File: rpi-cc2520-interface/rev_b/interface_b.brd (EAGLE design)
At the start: 30.5 x 39.5 mm, 5 parts, among them J1 PINHD-2X12/SMD, J2 PINHD-2X12/SMD

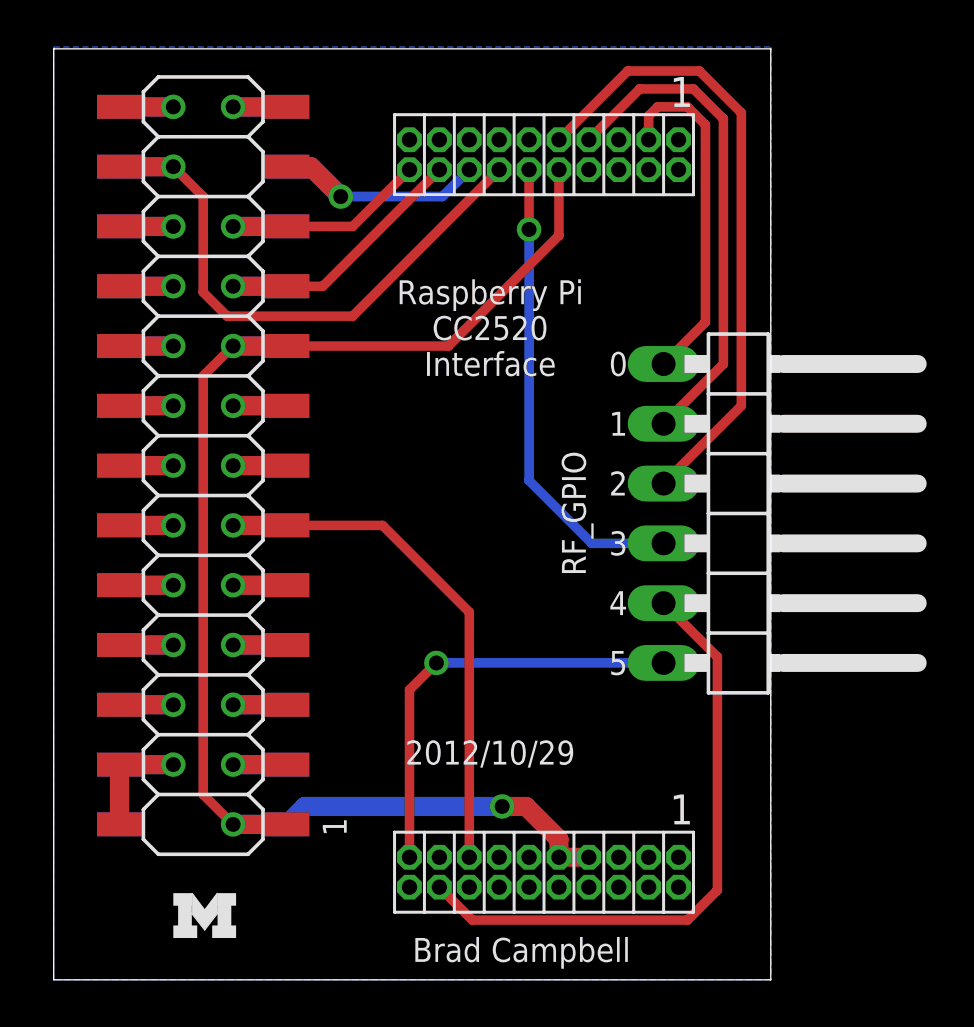
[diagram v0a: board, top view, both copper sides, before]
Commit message: new rpi-cc2520 board is routed. want to add pin labels
git-svn-id: svn+ssh://energy.eecs.umich.edu/svnroot/shed/projects/pi-router/eagle@2756 d5a83394-2863-40c7-9603-03341d4c7fdc
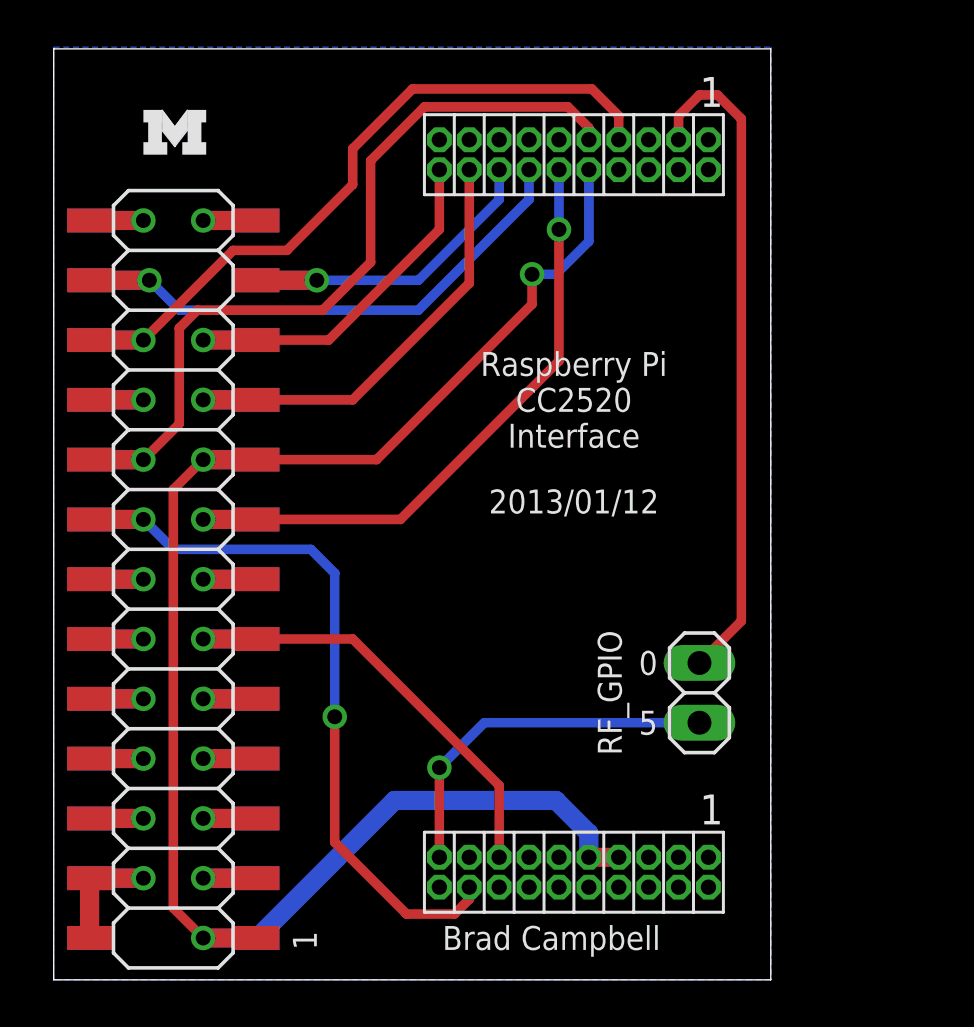
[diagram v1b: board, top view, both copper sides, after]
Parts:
- JP1: device pinhead:1X06/90 -> pinhead:1X02
- moved U$1 33.3 mm to (3.81, 35.1)
- moved JP1 7.96 mm to (27.4, 12.2), turned to 90 degrees
- moved J1 4.99 mm to (5.08, 17.0)
- moved J2 4.99 mm to (5.08, 17.0)
- moved EVM1 1.27 mm to (22.1, 19.8)
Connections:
- removed net GPIO22: J1.16, J2.15
- removed net GPIO23: J1.15, J2.16
- removed net GPIO24: J1.17, J2.18
- removed net GPIO25: J1.21, J2.22
- removed net RF_GPIO0: EVM1.P1_3, JP1.1
- removed net RF_GPIO1: EVM1.P1_7, JP1.2
- removed net RF_GPIO2: EVM1.P1_9, JP1.3
- removed net RF_GPIO3: EVM1.P1_12, JP1.4
- removed net RF_GPIO4: EVM1.P2_18, JP1.5
- removed net RF_GPIO5: EVM1.P2_19, JP1.6
- new net CCA: EVM1.P1_12, J1.16, J2.15
- new net CC_GPIO0: EVM1.P1_3, JP1.2
- new net CC_GPIO5: EVM1.P2_19, JP1.1
- new net FIFO: EVM1.P1_7, J1.21, J2.22
- new net FIFOP: EVM1.P1_9, J1.17, J2.18
- new net SFD: EVM1.P2_18, J1.15, J2.16
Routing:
- net FIFOP: track 0.00 -> 35.5 mm, vias 0 -> 1
- net SFD: track 0.00 -> 32.8 mm, vias 0 -> 2
- net FIFO: track 0.00 -> 31.6 mm, vias 0 -> 1
- net CC_GPIO0: track 0.00 -> 28.3 mm
- net CCA: track 0.00 -> 28.3 mm, vias 0 -> 2
- net RF_GPIO2: track 26.8 -> 0.00 mm
- net RF_GPIO4: track 26.1 -> 0.00 mm
- net RF_GPIO1: track 21.1 -> 0.00 mm
- net RF_GPIO3: track 20.0 -> 0.00 mm, vias 1 -> 0
- net RF_GPIO5: track 18.4 -> 0.00 mm, vias 1 -> 0
- net CC_GPIO5: track 0.00 -> 15.6 mm, vias 0 -> 1
- net RF_GPIO0: track 14.8 -> 0.00 mm
- net 3.3V: track 61.3 -> 71.6 mm
- net MOSI: track 13.1 -> 20.5 mm
- net MISO: track 10.8 -> 16.8 mm
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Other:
- board text added: "2013/01/12"
- board text removed: "2"
- board text removed: "2012/10/29"
- board text removed: "3"
- board text removed: "4"

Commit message: added LEDS and pin labels to interface board
git-svn-id: svn+ssh://energy.eecs.umich.edu/svnroot/shed/projects/pi-router/eagle@2765 d5a83394-2863-40c7-9603-03341d4c7fdc
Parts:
- added D1, D2, D3: (no value), SparkFun-LED:LED-0603
- added R1, R2, R3: (no value), rcl:R0603
- moved U$1 1.02 mm to (3.81, 36.1)
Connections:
- removed net 3.3V: EVM1.P1_10, EVM1.P2_7, EVM1.P2_9, J1.18, J1.2, J2.1, J2.17
- removed net GPIO18: J1.11, J2.12
- removed net GPIO27: J1.14, J2.13
- removed net GPIO4: J1.8, J2.7
- new net LED0: J1.8, J2.7, R1.1
- new net LED1: J1.11, J2.12, R2.1
- new net LED2: J1.14, J2.13, R3.1
- new net N$1: D1.C, R1.2
- new net N$2: D2.C, R2.2
- new net N$3: D3.C, R3.2
- new net VCC: D1.A, D2.A, D3.A, EVM1.P1_10, EVM1.P2_7, EVM1.P2_9, J1.18, J1.2, J2.1, J2.17
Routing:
- net VCC: track 0.00 -> 99.5 mm, vias 0 -> 3
- net 3.3V: track 71.6 -> 0.00 mm, vias 3 -> 0
- net LED2: track 0.00 -> 33.5 mm, vias 0 -> 3
- net LED1: track 0.00 -> 31.2 mm, vias 0 -> 3
- net LED0: track 0.00 -> 18.3 mm, vias 0 -> 2
- net GPIO18: track 4.57 -> 0.00 mm, vias 1 -> 0
- net GPIO4: track 4.57 -> 0.00 mm, vias 1 -> 0
- net GPIO27: track 4.57 -> 0.00 mm, vias 1 -> 0
- net N$2: track 0.00 -> 2.74 mm, vias 0 -> 1
- net N$1: track 0.00 -> 2.73 mm, vias 0 -> 1
- net N$3: track 0.00 -> 2.46 mm, vias 0 -> 1
- net SFD: track 32.8 -> 32.1 mm
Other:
- board text added: "2013/01/14"
- board text added: "3.3V"
- board text added: "5V"
- board text added: "CCA"
- board text added: "CE1"
- board text added: "CS"
- board text added: "FIFO"
- board text added: "FIFP"
- board text added: "G17"
- board text added: "GND"
- board text added: "LE1"
- board text added: "LED0"
- board text added: "LED2"
- board text added: "MISO"
- board text added: "MOSI"
- board text added: "RXD"
- board text added: "SCL"
- board text added: "SCLK"
- board text added: "SDA"
- board text added: "SFD"
- board text added: "TXD"
- board text removed: "2013/01/12"

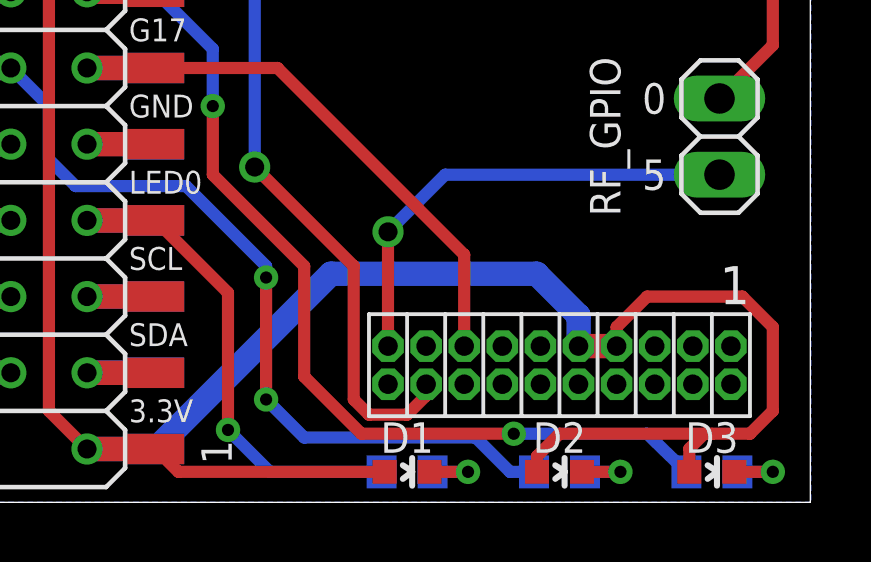
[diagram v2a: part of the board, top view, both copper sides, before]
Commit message: fixed an airwire
git-svn-id: svn+ssh://energy.eecs.umich.edu/svnroot/shed/projects/pi-router/eagle@2766 d5a83394-2863-40c7-9603-03341d4c7fdc
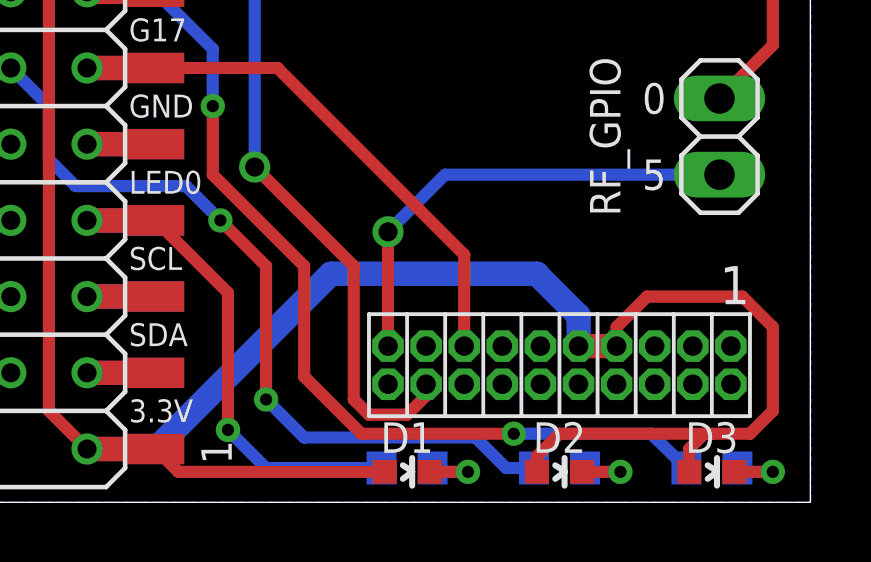
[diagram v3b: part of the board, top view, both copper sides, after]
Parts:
- moved R1 0.13 mm to (17.0, 1.14)
- moved R2 0.13 mm to (22.1, 1.14)
- moved R3 0.13 mm to (27.2, 1.14)
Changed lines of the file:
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@@
 <attribute name="VALUE" x="26.162" y="-0.0635" size="0.4064" layer="27"/>
 </element>
-<element name="R1" library="rcl" package="R0603" value="" x="17.018" y="1.016" smashed="yes" rot="MR180">
-<attribute name="NAME" x="17.018" y="1.778" size="1.016" layer="26" font="vector" ratio="12" rot="MR180" align="top-center"/>
-<attribute name="VALUE" x="16.383" y="2.921" size="1.27" layer="28" rot="MR180"/>
+<element name="R1" library="rcl" package="R0603" value="" x="17.018" y="1.143" smashed="yes" rot="MR180">
+<attribute name="NAME" x="17.018" y="1.905" size="1.016" layer="26" font="vector" ratio="12" rot="MR180" align="top-center"/>
+<attribute name="VALUE" x="16.383" y="3.048" size="1.27" layer="28" rot="MR180"/>
 </element>
-<element name="R2" library="rcl" package="R0603" value="" x="22.098" y="1.016" smashed="yes" rot="MR180">
-<attribute name="NAME" x="22.098" y="1.778" size="1.016" layer="26" font="vector" ratio="12" rot="MR180" align="top-center"/>
-<attribute name="VALUE" x="21.463" y="2.921" size="1.27" layer="28" rot="MR180"/>
+<element name="R2" library="rcl" package="R0603" value="" x="22.098" y="1.143" smashed="yes" rot="MR180">
+<attribute name="NAME" x="22.098" y="1.905" size="1.016" layer="26" font="vector" ratio="12" rot="MR180" align="top-center"/>
+<attribute name="VALUE" x="21.463" y="3.048" size="1.27" layer="28" rot="MR180"/>
 </element>
-<element name="R3" library="rcl" package="R0603" value="" x="27.178" y="1.016" smashed="yes" rot="MR180">
-<attribute name="NAME" x="27.178" y="1.778" size="1.016" layer="26" font="vector" ratio="12" rot="MR180" align="top-center"/>
-<attribute name="VALUE" x="26.543" y="2.921" size="1.27" layer="28" rot="MR180"/>
+<element name="R3" library="rcl" package="R0603" value="" x="27.178" y="1.143" smashed="yes" rot="MR180">
+<attribute name="NAME" x="27.178" y="1.905" size="1.016" layer="26" font="vector" ratio="12" rot="MR180" align="top-center"/>
+<attribute name="VALUE" x="26.543" y="3.048" size="1.27" layer="28" rot="MR180"/>
 </element>
 </elements>
@@
 <contactref element="D1" pad="C"/>
 <contactref element="R1" pad="2"/>
-<wire x1="17.868" y1="1.016" x2="17.78" y2="1.27" width="0.4064" layer="16"/>
-<wire x1="17.868" y1="1.016" x2="19.05" y2="1.016" width="0.4064" layer="16"/>
+<wire x1="17.868" y1="1.143" x2="17.78" y2="1.27" width="0.4064" layer="16"/>
 <via x="19.05" y="1.016" extent="1-16" drill="0.4064"/>
 <wire x1="19.05" y1="1.016" x2="17.768" y2="1.016" width="0.4064" layer="1"/>
+<wire x1="19.05" y1="1.016" x2="17.995" y2="1.016" width="0.4064" layer="16"/>
+<wire x1="17.995" y1="1.016" x2="17.868" y2="1.143" width="0.4064" layer="16"/>
 </signal>
 <signal name="N$2">
@@
 <wire x1="22.848" y1="1.016" x2="24.13" y2="1.016" width="0.4064" layer="1"/>
 <via x="24.13" y="1.016" extent="1-16" drill="0.4064"/>
-<wire x1="22.948" y1="1.016" x2="22.848" y2="1.27" width="0.4064" layer="16"/>
-<wire x1="22.948" y1="1.016" x2="24.13" y2="1.016" width="0.4064" layer="16"/>
+<wire x1="22.948" y1="1.143" x2="22.848" y2="1.27" width="0.4064" layer="16"/>
+<wire x1="24.13" y1="1.016" x2="23.075" y2="1.016" width="0.4064" layer="16"/>
+<wire x1="23.075" y1="1.016" x2="22.948" y2="1.143" width="0.4064" layer="16"/>
 </signal>
 <signal name="N$3">
@@
 <wire x1="27.928" y1="1.016" x2="29.21" y2="1.016" width="0.4064" layer="1"/>
 <via x="29.21" y="1.016" extent="1-16" drill="0.4064"/>
-<wire x1="28.028" y1="1.016" x2="29.21" y2="1.016" width="0.4064" layer="16"/>
+<wire x1="29.21" y1="1.016" x2="28.155" y2="1.016" width="0.4064" layer="16"/>
+<wire x1="28.155" y1="1.016" x2="28.028" y2="1.143" width="0.4064" layer="16"/>
 </signal>
 <signal name="VCC">
@@
 <via x="6.35" y="17.018" extent="1-16" drill="0.635"/>
 <wire x1="6.35" y1="17.018" x2="8.636" y2="17.018" width="0.8128" layer="1"/>
-<wire x1="26.328" y1="1.016" x2="25.019" y2="2.286" width="0.4064" layer="16"/>
-<wire x1="25.019" y1="2.286" x2="20.574" y2="2.286" width="0.4064" layer="16"/>
+<wire x1="26.328" y1="1.143" x2="25.146" y2="2.286" width="0.4064" layer="16"/>
+<wire x1="25.146" y1="2.286" x2="20.574" y2="2.286" width="0.4064" layer="16"/>
 <via x="20.574" y="2.286" extent="1-16" drill="0.4064"/>
 <wire x1="20.574" y1="2.286" x2="15.494" y2="2.286" width="0.4064" layer="1"/>
@@
 <wire x1="13.589" y1="2.159" x2="12.319" y2="3.429" width="0.4064" layer="16"/>
 <via x="12.319" y="3.429" extent="1-16" drill="0.4064"/>
-<wire x1="12.319" y1="3.429" x2="12.319" y2="7.493" width="0.4064" layer="1"/>
-<via x="12.319" y="7.493" extent="1-16" drill="0.4064"/>
-<wire x1="12.319" y1="7.493" x2="12.319" y2="7.874" width="0.4064" layer="16"/>
-<wire x1="12.319" y1="7.874" x2="9.652" y2="10.541" width="0.4064" layer="16"/>
+<wire x1="12.319" y1="3.429" x2="12.319" y2="7.874" width="0.4064" layer="1"/>
+<wire x1="12.319" y1="7.874" x2="10.795" y2="9.398" width="0.4064" layer="1"/>
+<via x="10.795" y="9.398" extent="1-16" drill="0.4064"/>
+<wire x1="10.795" y1="9.398" x2="9.652" y2="10.541" width="0.4064" layer="16"/>
 <wire x1="9.652" y1="10.541" x2="5.969" y2="10.541" width="0.4064" layer="16"/>
 <wire x1="5.969" y1="10.541" x2="5.08" y2="11.43" width="0.4064" layer="16"/>
 <wire x1="5.08" y1="11.43" x2="5.08" y2="13.208" width="0.4064" layer="16"/>
 <wire x1="5.08" y1="13.208" x2="3.81" y2="14.478" width="0.4064" layer="16"/>
-<wire x1="21.248" y1="1.016" x2="20.447" y2="1.016" width="0.4064" layer="16"/>
-<wire x1="20.447" y1="1.016" x2="19.304" y2="2.159" width="0.4064" layer="16"/>
+<wire x1="21.248" y1="1.143" x2="20.32" y2="1.143" width="0.4064" layer="16"/>
+<wire x1="20.32" y1="1.143" x2="19.304" y2="2.159" width="0.4064" layer="16"/>
 <wire x1="19.304" y1="2.159" x2="13.589" y2="2.159" width="0.4064" layer="16"/>
 </signal>
@@
 <wire x1="11.049" y1="2.413" x2="11.049" y2="6.985" width="0.4064" layer="1"/>
 <wire x1="11.049" y1="6.985" x2="8.636" y2="9.398" width="0.4064" layer="1"/>
-<wire x1="16.168" y1="1.016" x2="12.446" y2="1.016" width="0.4064" layer="16"/>
-<wire x1="12.446" y1="1.016" x2="11.049" y2="2.413" width="0.4064" layer="16"/>
+<wire x1="16.168" y1="1.143" x2="12.319" y2="1.143" width="0.4064" layer="16"/>
+<wire x1="12.319" y1="1.143" x2="11.049" y2="2.413" width="0.4064" layer="16"/>
 <via x="11.049" y="2.413" extent="1-16" drill="0.4064"/>
 </signal>
